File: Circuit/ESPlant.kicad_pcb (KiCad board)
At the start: 2 copper layers, 50 x 100 mm, 72 parts, among them P1 SOIL, P101 CONN_DIGITAL, P102 CONN_ANALOG, P103 CONN_SERIAL, P104 CONN_I2C, P105 SOLAR, P106 USB_5PIN_SHELL, P109 CONN_PWR, P110 CONN_01X05, P111 UV, P112 TEMP, P113 NEOPIXEL, P114 PIR, Q101 FDN340P, Q201 FDN340P, Q202 FDN340P, Q203 FDN340P, SW101 RESET, SW102 PRGM, SW103 RESET, U101 STM32F042F, U103 ESP-12E, U201 CN3063, U202 MCP6002, U301 BME280, U302 ADXL345

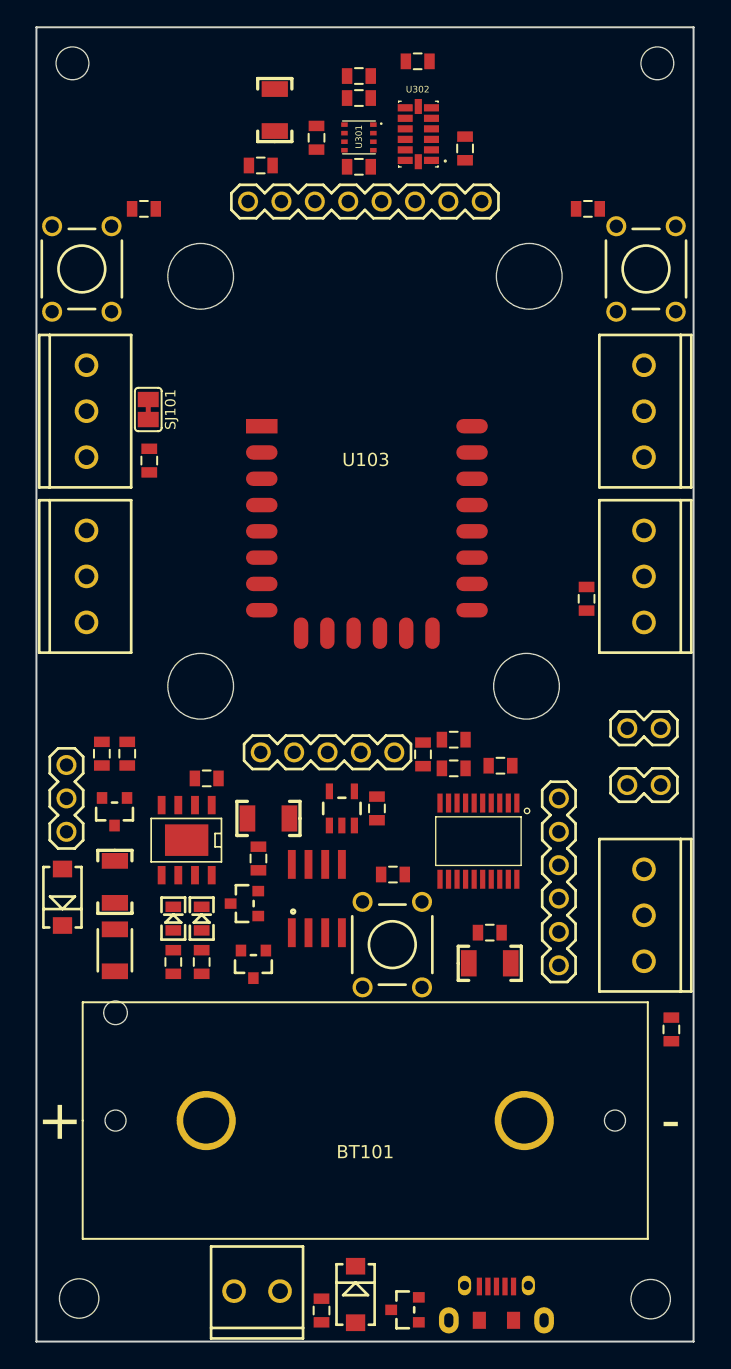
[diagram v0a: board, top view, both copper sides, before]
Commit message: 5 Vias, no text.
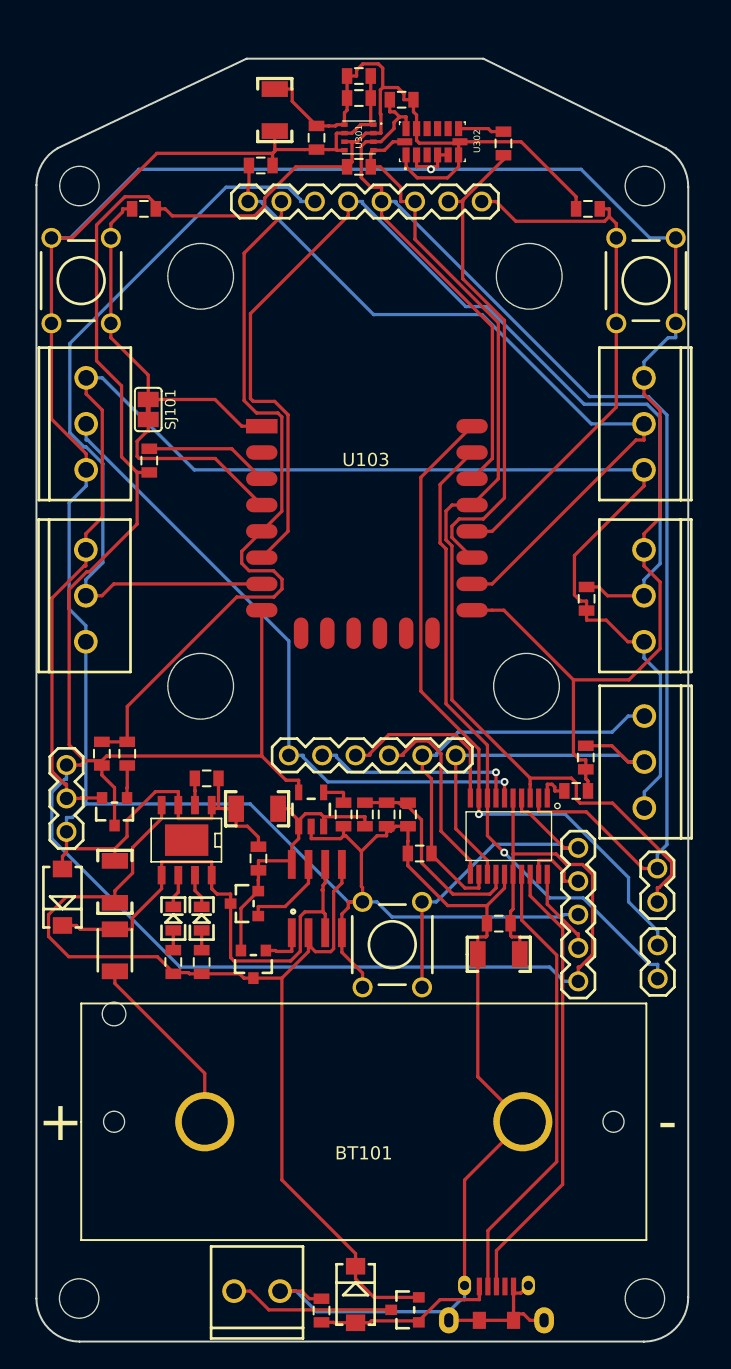
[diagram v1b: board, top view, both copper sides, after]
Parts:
- LED201: value DONE -> LED_DONE
- LED202: value CHRG -> LED_CHRG
- REF05, REF06: value MountingHole_2-5mm -> MOUNT; footprint Mounting_Holes:MountingHole_2-5mm -> Mounting_Holes:MountingHole_3mm
- REF07, REF08: value MountingHole_2-5mm -> MOUNT
- REG101: value SPX3819M5-3.3 -> SPX3819M5
- moved P110 29.8 mm to (70.7, 107.4), turned to 90 degrees
- moved R103 21.7 mm to (71.3, 90.4)
- moved P102 20.8 mm to (48.7, 90.2), turned to 0 degrees
- moved P104 13.4 mm to (76.7, 101.3), turned to 90 degrees
- moved P103 12.2 mm to (76.7, 104.6), turned to 270 degrees
- moved P1 11.7 mm to (75.7, 90.7)
- moved REF06 9.39 mm to (75.8, 46.9)
- moved REF05 9.35 mm to (32.7, 46.9)
- moved C104 7.64 mm to (56.1, 94.7), turned to 270 degrees
- moved R107 6.36 mm to (54.5, 94.7)
- moved R101 6.07 mm to (70.5, 92.9), turned to 0 degrees
- moved R108 4.94 mm to (57.7, 94.7), turned to 270 degrees
- moved R301 3.17 mm to (57.3, 40.3)
- moved R105 2.95 mm to (65.0, 43.6)
- moved R102 2.59 mm to (58.6, 97.7)
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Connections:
- LED201 pad K: /Power/~CHRG -> /Power/~DONE
- U201 pad 6: /Power/~CHRG -> /Power/~DONE
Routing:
- net GND: track 0.00 -> 371.6 mm, vias 0 -> 1
- net +3V3: track 0.00 -> 236.3 mm
- net /VCC_SENS: track 0.00 -> 115.8 mm
- net /I2C Sensors/I2C_SDA: track 0.00 -> 113.1 mm
- net /GPIO12: track 0.00 -> 82.5 mm
- net /I2C Sensors/I2C_SCL: track 0.00 -> 80.0 mm
- net /Power/VIN: track 0.00 -> 79.8 mm
- net /GPIO15: track 0.00 -> 58.8 mm
- net /GPIO13: track 0.00 -> 58.7 mm
- net /GPIO14: track 0.00 -> 56.5 mm
- net /STM_RXD: track 0.00 -> 52.4 mm, vias 0 -> 1
- net /ADC0: track 0.00 -> 50.2 mm, vias 0 -> 1
- net /STM_TXD: track 0.00 -> 49.8 mm, vias 0 -> 1
- net /GPIO0: track 0.00 -> 41.4 mm
- net /Power/VBAT: track 0.00 -> 39.5 mm
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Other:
- board size 50 x 100 mm -> 49.6 x 97.6 mm

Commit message: Added text.
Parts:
- P103: value CONN_SERIAL -> SERIAL
- P104: value CONN_I2C -> I2C
- P109: value CONN_PWR -> PWR
- P110: value CONN_01X05 -> STM_PGM
- moved R109 3.38 mm to (43.2, 45.7), turned to 90 degrees
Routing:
- net GND: track 371.6 -> 375.3 mm
- net /GPIO14: track 56.5 -> 58.6 mm
- net +3V3: track 236.3 -> 236.8 mm
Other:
- board text added: "+"
- board text added: "+3v3"
- board text added: "-"
- board text added: "ADC0"
- board text added: "ADC1"
- board text added: "ADC2"
- board text added: "ADC3"
- board text added: "CONN_ANALOG"
- board text added: "CONN_DIGITAL"
- board text added: "ESPlant - Version 1.0 https://github.com/mage0r/ESPlant Designed by: John Spencer and Angus Gratton Open Hardware MiniConf, LinuxConf, Geelong, 2016 Made at hackmelbourne.org"
- board text added: "GND"
- board text added: "GPIO12"
- board text added: "GPIO13"
- board text added: "GPIO14"
- board text added: "GPIO15"
- board text added: "GPIO2"
- board text added: "I2C"
- board text added: "I2C_SCL"
- board text added: "I2C_SDA"
- board text added: "NEOPIXEL"
- board text added: "PIR"
- board text added: "PWR"
- board text added: "RST"
- board text added: "RXD"
- board text added: "SCL"
- board text added: "SDA"
- board text added: "SERIAL"
- board text added: "SOIL"
- board text added: "SOIL_1"
- board text added: "SOIL_2"
- board text added: "SOLAR"
- board text added: "STM_PGM"
- board text added: "SWCLK"
- board text added: "SWDIO"
- board text added: "TEMP"
- board text added: "TXD"
- board text added: "UV"
- board text added: "VCC"

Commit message: Updated the silkscreen text
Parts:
- moved P103 0.76 mm to (76.7, 103.9)
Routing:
- net /STM_TXD: track 49.8 -> 49.0 mm
- net /STM_RXD: track 52.4 -> 51.7 mm
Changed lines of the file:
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@@
       (effects (font (size 1 1) (thickness 0.15)))
     )
-    (fp_text value Battery (at 0 -2.4) (layer F.Fab)
+    (fp_text value Battery (at 0 -2.4) (layer F.SilkS)
       (effects (font (size 1 1) (thickness 0.15)))
     )
@@
       (effects (font (size 0.4064 0.4064) (thickness 0.03048)))
     )
-    (fp_text value SOIL (at 4.2164 -4.2164 90) (layer Eco1.User)
+    (fp_text value SOIL (at 4.2164 -4.2164 90) (layer F.SilkS)
       (effects (font (size 1 1) (thickness 0.25)))
     )
@@
       (effects (font (size 0.6 0.6) (thickness 0.1)))
     )
-    (fp_text value CONN_DIGITAL (at 8.9408 -2.6924 180) (layer Eco1.User)
+    (fp_text value CONN_DIGITAL (at 8.9408 -2.6924 180) (layer F.SilkS)
       (effects (font (size 0.6 0.6) (thickness 0.1)))
     )
@@
   )
   (module FT:1X02 (layer F.Cu)
-    (at 76.7334 104.648 270)
+    (at 76.708 103.88854 270)
     (fp_text reference P103 (at 4.191 0 360) (layer Eco1.User)
       (effects (font (size 0.3 0.3) (thickness 0.075)))
     )
-    (fp_text value SERIAL (at 1.1176 1.8542 270) (layer Eco1.User)
+    (fp_text value SERIAL (at 1.1176 1.8542 270) (layer F.SilkS)
       (effects (font (size 0.6 0.6) (thickness 0.1)))
     )
@@
       (effects (font (size 0.6 0.6) (thickness 0.1)))
     )
-    (fp_text value SOLAR (at -2.30124 -0.03516 90) (layer Eco1.User)
+    (fp_text value SOLAR (at -2.30124 -0.03516 90) (layer F.SilkS)
       (effects (font (size 0.6 0.6) (thickness 0.1)))
     )
@@
       (effects (font (size 0.4064 0.4064) (thickness 0.03048)))
     )
-    (fp_text value UV (at -4.3688 -4.5466 270) (layer Eco1.User)
+    (fp_text value UV (at -4.3688 -4.5466 270) (layer F.SilkS)
       (effects (font (size 1 1) (thickness 0.2)))
     )
@@
       (effects (font (size 0.4064 0.4064) (thickness 0.03048)))
     )
-    (fp_text value TEMP (at 3.60172 -4.20624 90) (layer Eco1.User)
+    (fp_text value TEMP (at 3.60172 -4.20624 90) (layer F.SilkS)
       (effects (font (size 1 1) (thickness 0.25)))
     )
@@
       (effects (font (size 0.4064 0.4064) (thickness 0.03048)))
     )
-    (fp_text value NEOPIXEL (at 0 -4.2926 270) (layer Eco1.User)
+    (fp_text value NEOPIXEL (at 0 -4.2926 270) (layer F.SilkS)
       (effects (font (size 1 1) (thickness 0.25)))
     )
@@
       (effects (font (size 0.4064 0.4064) (thickness 0.03048)))
     )
-    (fp_text value PIR (at 3.6703 -4.2926 90) (layer Eco1.User)
+    (fp_text value PIR (at 3.6703 -4.2926 90) (layer F.SilkS)
       (effects (font (size 1 1) (thickness 0.25)))
     )
@@
       (effects (font (size 0.6 0.6) (thickness 0.1)))
     )
-    (fp_text value RESET (at 0 3.556 90) (layer Eco1.User)
+    (fp_text value RESET (at 0 3.556 90) (layer F.SilkS)
       (effects (font (size 0.6 0.6) (thickness 0.1)))
     )
@@
       (effects (font (size 0.6 0.6) (thickness 0.1)))
     )
-    (fp_text value PRGM (at 0 3.556 270) (layer Eco1.User)
+    (fp_text value PRGM (at 0 3.556 270) (layer F.SilkS)
       (effects (font (size 0.6 0.6) (thickness 0.1)))
     )
@@
       (effects (font (size 0.6 0.6) (thickness 0.1)))
     )
-    (fp_text value RESET (at 0 3.6068 270) (layer Eco1.User)
+    (fp_text value RESET (at 0 3.6068 90) (layer F.SilkS)
       (effects (font (size 0.6 0.6) (thickness 0.1)))
     )
@@
   (module FT:1X02 (layer F.Cu)
     (at 76.708 101.346 90)
-    (fp_text reference P104 (at -1.651 0 180) (layer Eco1.User)
+    (fp_text reference P104 (at 4.25704 0 180) (layer Eco1.User)
       (effects (font (size 0.3 0.3) (thickness 0.075)))
     )
-    (fp_text value I2C (at 1.18872 -1.8288 90) (layer Eco1.User)
+    (fp_text value I2C (at 1.18872 -1.8288 90) (layer F.SilkS)
       (effects (font (size 0.6 0.6) (thickness 0.1)))
     )
@@
       (effects (font (size 0.6 0.6) (thickness 0.1)))
     )
-    (fp_text value CONN_ANALOG (at 6.4262 1.8034) (layer Eco1.User)
+    (fp_text value CONN_ANALOG (at 6.4262 1.8034) (layer F.SilkS)
       (effects (font (size 0.6 0.6) (thickness 0.1)))
     )
@@
     (effects (font (size 0.6 0.6) (thickness 0.1)) (justify mirror))
   )
-  (gr_text "SERIAL\n" (at 74.8792 105.91546 90) (layer B.SilkS)
+  (gr_text "SERIAL\n" (at 74.85888 105.0798 90) (layer B.SilkS)
     (effects (font (size 0.6 0.6) (thickness 0.1)) (justify mirror))
   )
@@
   (segment (start 62.609 65.151) (end 58.7116 69.0484) (width 0.25) (layer F.Cu) (net 28))
   (segment (start 63.13 93.4422) (end 63.13 94.4925) (width 0.25) (layer F.Cu) (net 28))
-  (segment (start 76.7334 104.648) (end 76.7334 103.5607) (width 0.25) (layer B.Cu) (net 28))
+  (segment (start 76.708 103.88854) (end 76.7334 103.5607) (width 0.25) (layer B.Cu) (net 28) (status 10))
   (segment (start 69.693 94.6726) (end 63.13 94.6726) (width 0.25) (layer B.Cu) (net 28))
   (segment (start 74.5188 99.4984) (end 69.693 94.6726) (width 0.25) (layer B.Cu) (net 28))
@@
   (segment (start 63.78 96.3109) (end 63.78 93.4422) (width 0.25) (layer F.Cu) (net 29))
   (segment (start 65.0589 97.5898) (end 63.78 96.3109) (width 0.25) (layer F.Cu) (net 29))
-  (segment (start 76.7334 107.188) (end 76.7334 106.1007) (width 0.25) (layer B.Cu) (net 29))
+  (segment (start 76.708 106.42854) (end 76.7334 106.1007) (width 0.25) (layer B.Cu) (net 29) (status 10))
   (segment (start 46.99082 132.385) (end 45.56782 130.962) (width 0.25) (layer F.Cu) (net 30))
   (segment (start 56.4566 132.385) (end 46.99082 132.385) (width 0.25) (layer F.Cu) (net 30))
